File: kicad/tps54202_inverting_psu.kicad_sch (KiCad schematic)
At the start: 19 parts, among them J5 PowerConnector, U1 TPS54202DDC

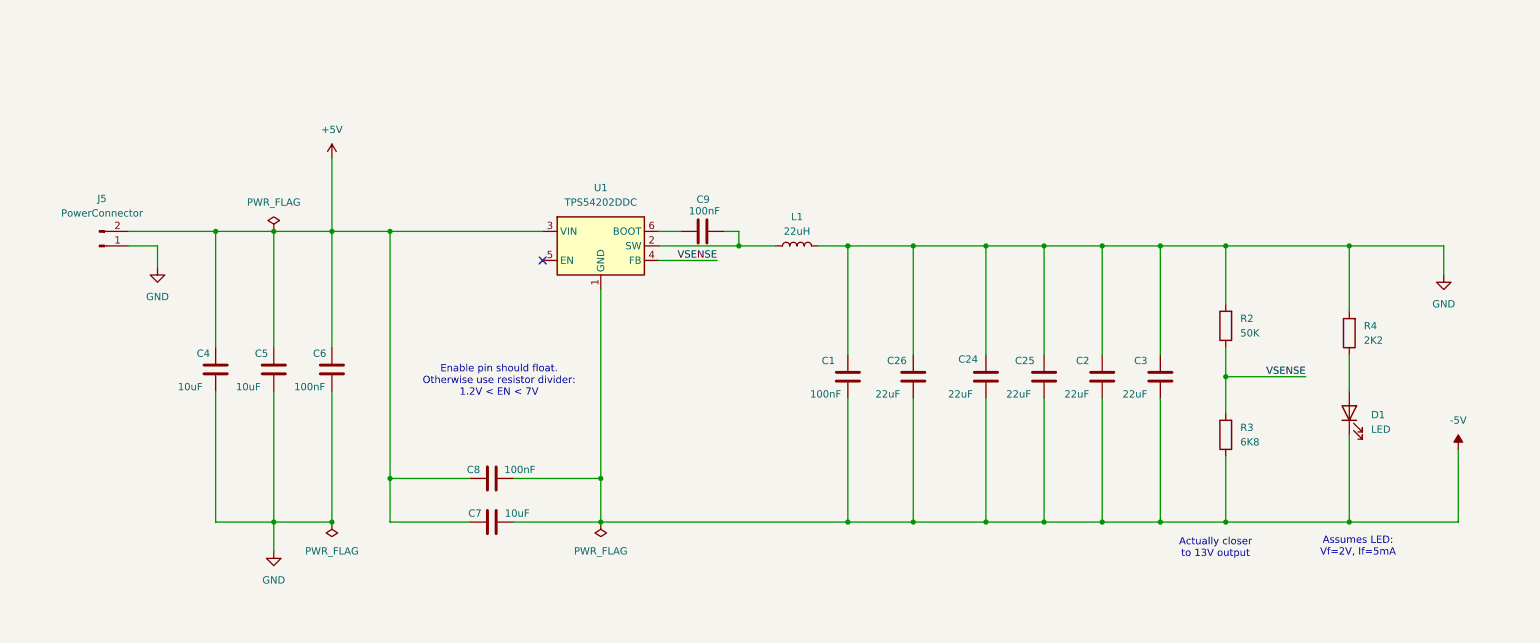
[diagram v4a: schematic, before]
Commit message: Revert "changed voltage rails to +/-5V; changed PSU feedback resistor to provide -5V"
This reverts commit 87719da26a309bbde2d2f76146bcb1e510287c62.
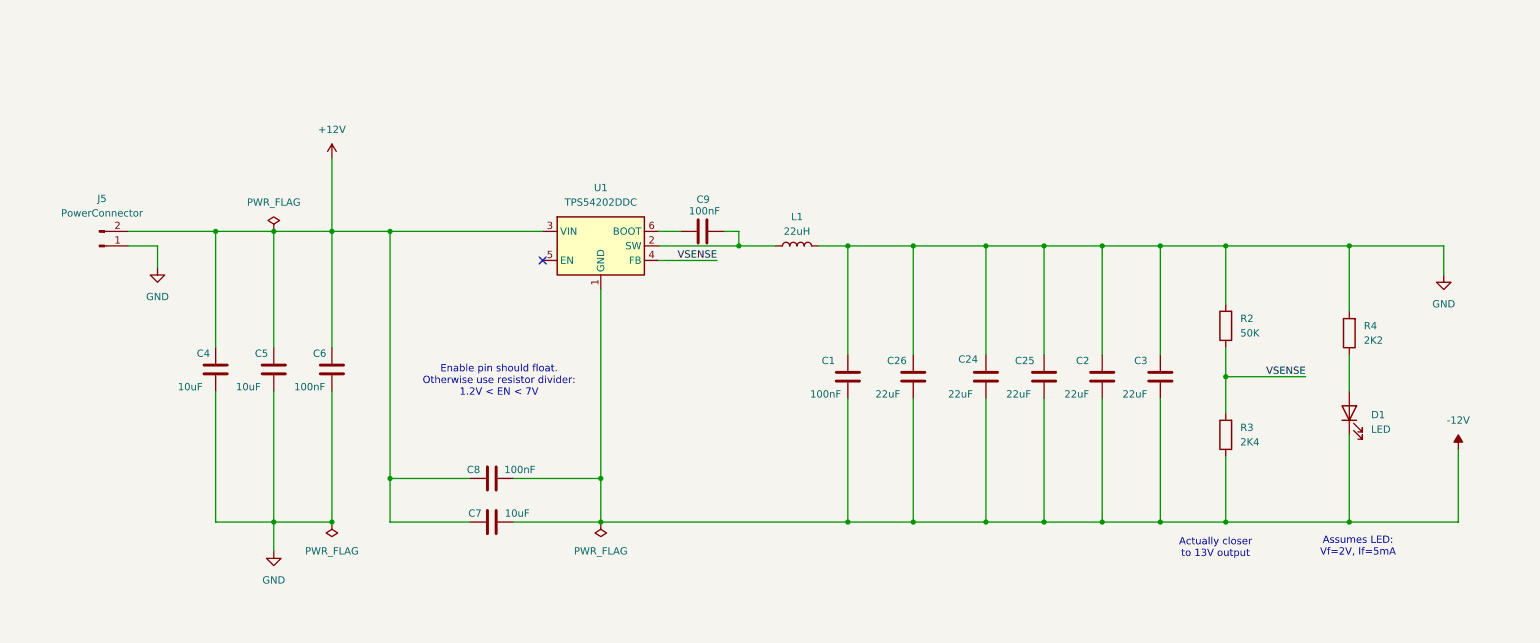
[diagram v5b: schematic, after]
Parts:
- R3: value 6K8 -> 2K4
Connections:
- net +5V renamed +12V
- net -5V renamed -12V
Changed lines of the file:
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@@
 			)
 		)
-		(property "Value" "6K8"
+		(property "Value" "2K4"
 			(at 229.87 95.2499 0)
 			(effects
@@
 	)
 	(symbol
+		(lib_id "power:+12V")
+		(at 71.12 45.72 0)
+		(unit 1)
+		(exclude_from_sim no)
+		(in_bom yes)
+		(on_board yes)
+		(dnp no)
+		(fields_autoplaced yes)
+		(property "Reference" "#PWR027"
+			(at 71.12 49.53 0)
+			(effects
+				(font
+					(size 1.27 1.27)
+				)
+				(hide yes)
+			)
+		)
+		(property "Value" "+12V"
+			(at 71.12 40.64 0)
+			(effects
+				(font
+					(size 1.27 1.27)
+				)
+			)
+		)
+		(property "Footprint" ""
+			(at 71.12 45.72 0)
+			(effects
+				(font
+					(size 1.27 1.27)
+				)
+				(hide yes)
+			)
+		)
+		(property "Datasheet" ""
+			(at 71.12 45.72 0)
+			(effects
+				(font
+					(size 1.27 1.27)
+				)
+				(hide yes)
+			)
+		)
+		(property "Description" "Power symbol creates a global label with name \"+12V\""
+			(at 71.12 45.72 0)
+			(effects
+				(font
+					(size 1.27 1.27)
+				)
+				(hide yes)
+			)
+		)
+		(pin "1"
+		)
+		(instances
+			(project "Tiny4xPoweredStereoMixer"
+				(path "/68c4b081-ef47-4ba5-a55f-4ef66cb2b598/94012ff5-5e55-42ff-bfc1-d0e6ccd3728b"
+					(reference "#PWR027")
+					(unit 1)
+				)
+			)
+		)
+	)
+	(symbol
 		(lib_id "power:GND")
 		(at 60.96 114.3 0)
@@
 	)
 	(symbol
-		(lib_id "power:-5V")
-		(at 267.97 96.52 0)
-		(unit 1)
-		(exclude_from_sim no)
-		(in_bom yes)
-		(on_board yes)
-		(dnp no)
-		(fields_autoplaced yes)
-		(property "Reference" "#PWR05"
-			(at 267.97 100.33 0)
-			(effects
-				(font
-					(size 1.27 1.27)
-				)
-				(hide yes)
-			)
-		)
-		(property "Value" "-5V"
-			(at 267.97 91.44 0)
-			(effects
-				(font
-					(size 1.27 1.27)
-				)
-			)
-		)
-		(property "Footprint" ""
-			(at 267.97 96.52 0)
-			(effects
-				(font
-					(size 1.27 1.27)
-				)
-				(hide yes)
-			)
-		)
-		(property "Datasheet" ""
-			(at 267.97 96.52 0)
-			(effects
-				(font
-					(size 1.27 1.27)
-				)
-				(hide yes)
-			)
-		)
-		(property "Description" "Power symbol creates a global label with name \"-5V\""
-			(at 267.97 96.52 0)
-			(effects
-				(font
-					(size 1.27 1.27)
-				)
-				(hide yes)
-			)
-		)
-		(pin "1"
-		)
-		(instances
-			(project "Tiny4xPoweredStereoMixer"
-				(path "/68c4b081-ef47-4ba5-a55f-4ef66cb2b598/94012ff5-5e55-42ff-bfc1-d0e6ccd3728b"
-					(reference "#PWR05")
-					(unit 1)
-				)
-			)
-		)
-	)
-	(symbol
 		(lib_id "Device:L")
 		(at 152.4 60.96 90)
@@
 	)
 	(symbol
-		(lib_id "power:+5V")
-		(at 71.12 45.72 0)
-		(unit 1)
-		(exclude_from_sim no)
-		(in_bom yes)
-		(on_board yes)
-		(dnp no)
-		(fields_autoplaced yes)
-		(property "Reference" "#PWR06"
-			(at 71.12 49.53 0)
-			(effects
-				(font
-					(size 1.27 1.27)
-				)
-				(hide yes)
-			)
-		)
-		(property "Value" "+5V"
-			(at 71.12 40.64 0)
-			(effects
-				(font
-					(size 1.27 1.27)
-				)
-			)
-		)
-		(property "Footprint" ""
-			(at 71.12 45.72 0)
-			(effects
-				(font
-					(size 1.27 1.27)
-				)
-				(hide yes)
-			)
-		)
-		(property "Datasheet" ""
-			(at 71.12 45.72 0)
-			(effects
-				(font
-					(size 1.27 1.27)
-				)
-				(hide yes)
-			)
-		)
-		(property "Description" "Power symbol creates a global label with name \"+5V\""
-			(at 71.12 45.72 0)
-			(effects
-				(font
-					(size 1.27 1.27)
-				)
-				(hide yes)
-			)
-		)
-		(pin "1"
-		)
-		(instances
-			(project "Tiny4xPoweredStereoMixer"
-				(path "/68c4b081-ef47-4ba5-a55f-4ef66cb2b598/94012ff5-5e55-42ff-bfc1-d0e6ccd3728b"
-					(reference "#PWR06")
-					(unit 1)
-				)
-			)
-		)
-	)
-	(symbol
 		(lib_id "power:GND")
 		(at 265.43 66.04 0)
@@
 					(unit 1)
 				)
+			)
+		)
+	)
+	(symbol
+		(lib_id "power:-12V")
+		(at 267.97 96.52 0)
+		(unit 1)
+		(exclude_from_sim no)
+		(in_bom yes)
+		(on_board yes)
+		(dnp no)
+		(fields_autoplaced yes)
+		(property "Reference" "#PWR031"
+			(at 267.97 100.33 0)
+			(effects
+				(font
+					(size 1.27 1.27)
+				)
+				(hide yes)
+			)
+		)
+		(property "Value" "-12V"
+			(at 267.97 91.44 0)
+			(effects
+				(font
+					(size 1.27 1.27)
+				)
+			)
+		)
+		(property "Footprint" ""
+			(at 267.97 96.52 0)
+			(effects
+				(font
+					(size 1.27 1.27)
+				)
+				(hide yes)
+			)
+		)
+		(property "Datasheet" ""
+			(at 267.97 96.52 0)
+			(effects
+				(font
+					(size 1.27 1.27)
+				)
+				(hide yes)
+			)
+		)
+		(property "Description" "Power symbol creates a global label with name \"-12V\""
+			(at 267.97 96.52 0)
+			(effects
+				(font
+					(size 1.27 1.27)
+				)
+				(hide yes)
+			)
+		)
+		(pin "1"
+		)
+		(instances
+			(project "Tiny4xPoweredStereoMixer"
+				(path "/68c4b081-ef47-4ba5-a55f-4ef66cb2b598/94012ff5-5e55-42ff-bfc1-d0e6ccd3728b"
+					(reference "#PWR031")
+					(unit 1)
+				)

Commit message: PSU now uses +/- 2.5V; Added barrel jack; updated layout
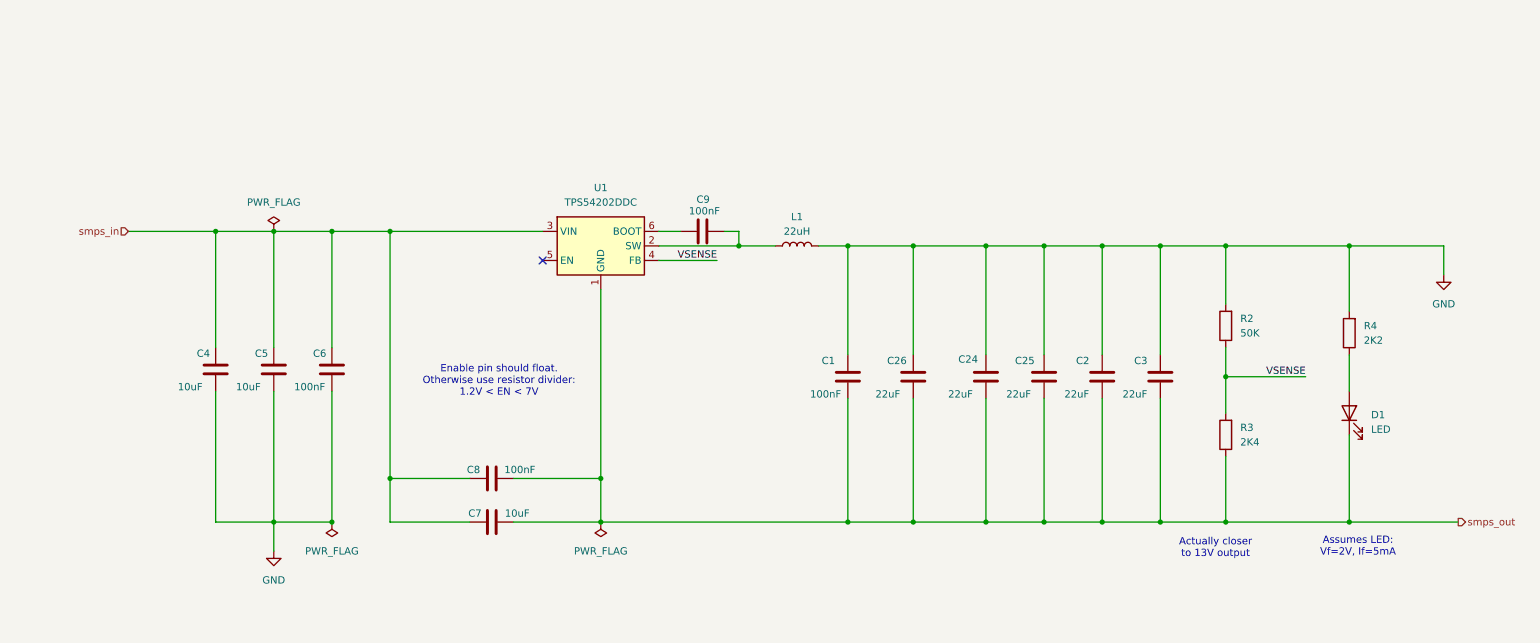
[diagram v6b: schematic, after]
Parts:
- removed J5: PowerConnector, Connector_Molex:Molex_KK-254_AE-6410-02A_1x02_P2.54mm_Vertical, symbol Connector:Conn_01x02_Pin
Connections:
- net +12V renamed smps_in
- net -12V renamed smps_out
